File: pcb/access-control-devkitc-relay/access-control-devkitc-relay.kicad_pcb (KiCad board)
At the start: 2 copper layers, 21.2 x 56 mm, 12 parts, among them K1 G5LE-1

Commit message: Update with values
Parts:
- added D3: D_Zener, Diode_THT:D_DO-41_SOD81_P10.16mm_Horizontal, F.Cu at (19.0, 27.4)
- moved J_COIL_LOW1 15.7 mm to (18.9, 34.2)
- renumbered J_COIL_LOW1 to J_COIL_HIGH1, J_COIL_LOW2 to J_COIL_LOW1
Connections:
- J_COIL_LOW1 pad 1: Net-(D1-A) -> Net-(D3-K)
- K1 pad 2: Net-(D1-A) -> Net-(D3-K)
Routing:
- net Net-(D3-K): track 0.00 -> 36.2 mm
- net Net-(D1-A): track 24.7 -> 2.61 mm

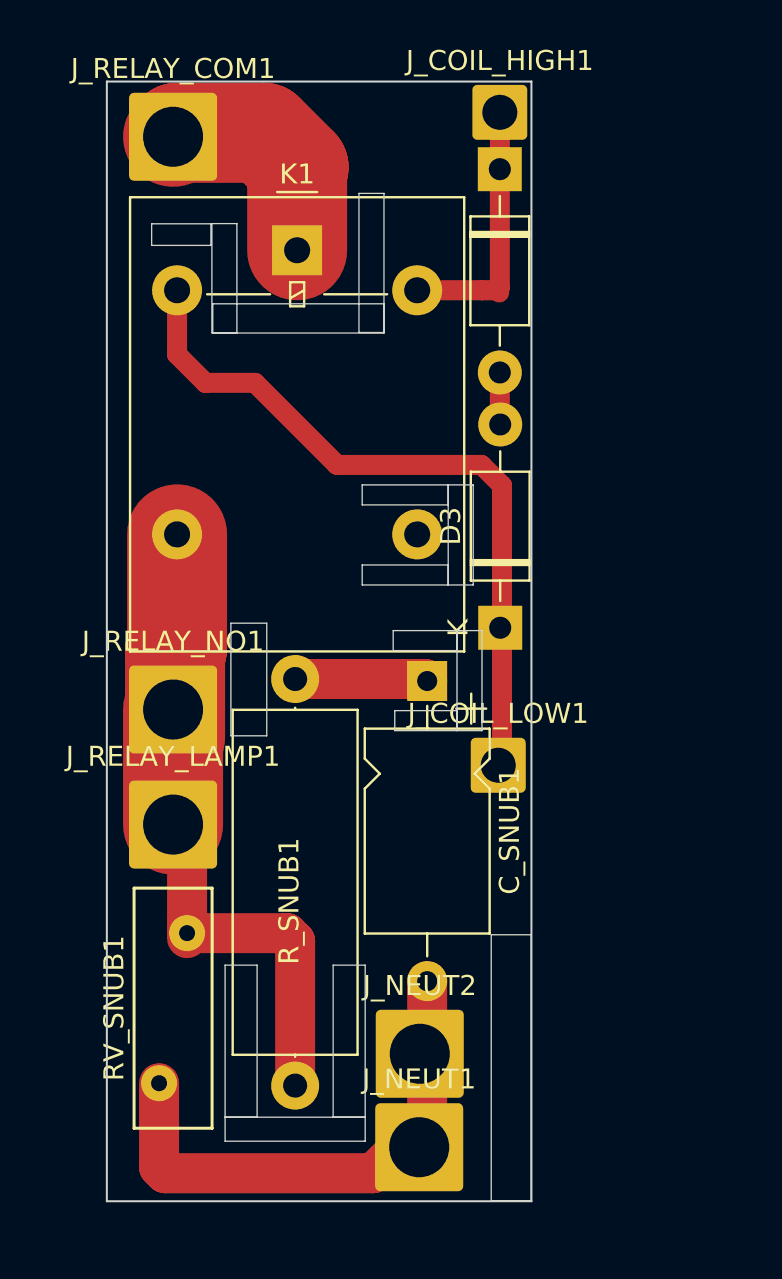
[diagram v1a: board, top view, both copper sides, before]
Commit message: Contactor interface and current sensor (part only)
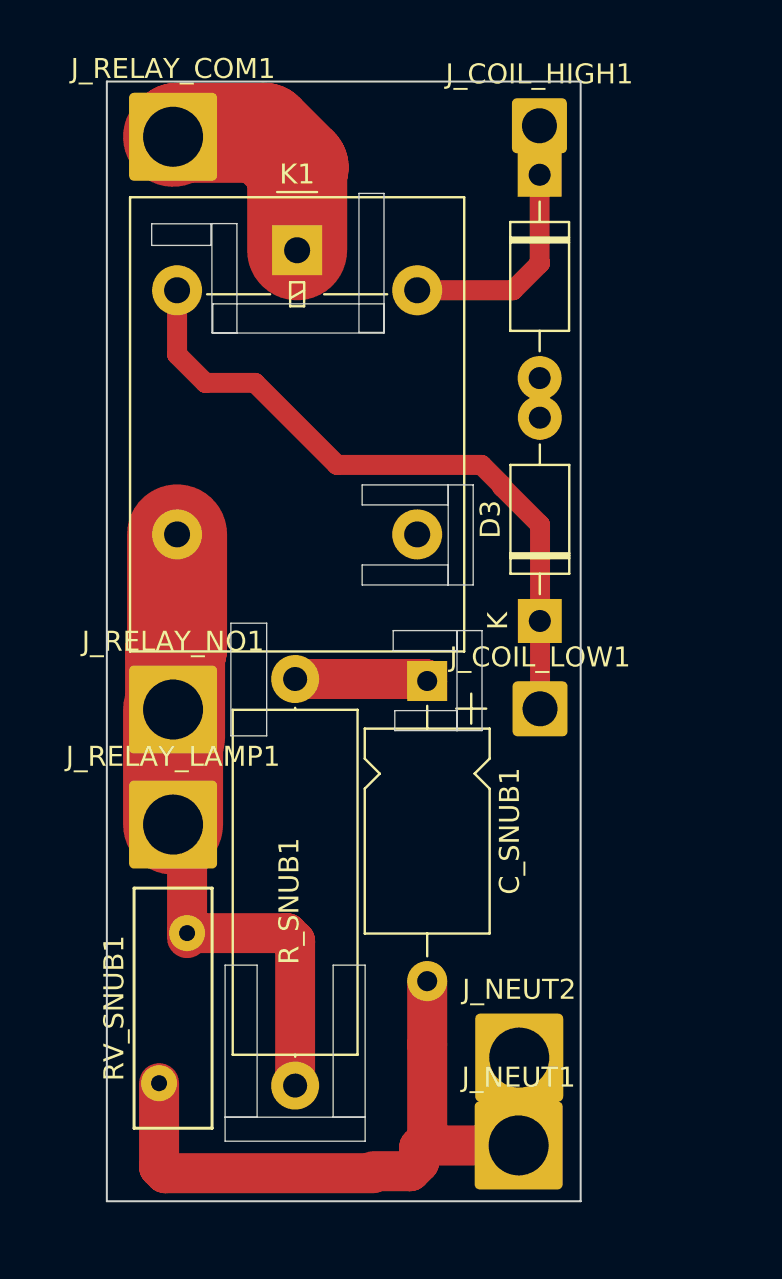
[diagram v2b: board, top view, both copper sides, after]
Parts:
- moved J_NEUT2 4.97 mm to (19.9, 48.8)
- moved J_NEUT1 4.97 mm to (19.9, 53.2)
- moved J_COIL_LOW1 3.51 mm to (21.0, 31.4)
- moved J_COIL_HIGH1 2.09 mm to (21.0, 2.27)
- moved D1 2.01 mm to (21.0, 4.72)
- moved D3 2.01 mm to (21.0, 27.0)
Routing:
- net NEUT: track 25.0 -> 36.1 mm
- net Net-(D3-K): track 36.2 -> 34.1 mm
- net +5V: track 12.8 -> 14.0 mm
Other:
- board size 21.2 x 56 mm -> 23.7 x 56 mm

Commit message: Fixes to relief, JST connectors for SMT board
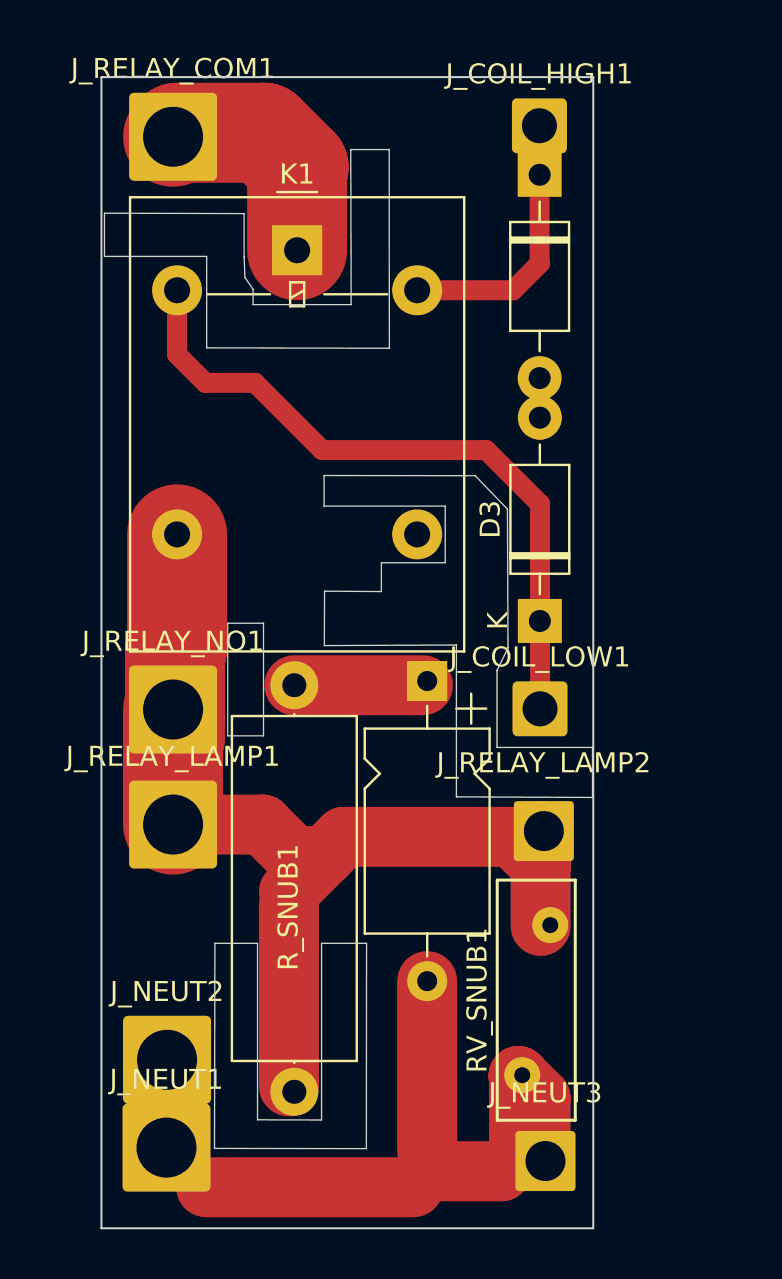
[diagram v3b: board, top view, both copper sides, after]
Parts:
- added J_NEUT3: Conn_01x01_Socket, Connector_Wire:SolderWire-2.5sqmm_1x01_D2.4mm_OD4.4mm, F.Cu at (21.3, 54.0)
- added J_RELAY_LAMP2: Conn_01x01_Socket, Connector_Wire:SolderWire-2.5sqmm_1x01_D2.4mm_OD4.4mm, F.Cu at (21.2, 37.5)
- moved RV_SNUB1 18.2 mm to (21.5, 42.2)
- moved J_NEUT1 17.6 mm to (2.32, 53.3)
- moved J_NEUT2 17.6 mm to (2.35, 49.0)
- moved R_SNUB1 0.31 mm to (8.71, 50.5)
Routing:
- net Net-(J_RELAY_LAMP1-Pin_1): track 36.5 -> 55.0 mm
- net Net-(D1-A): track 2.61 -> 4.59 mm
- net NEUT: track 36.1 -> 38.0 mm
- net Net-(D3-K): track 34.1 -> 34.7 mm
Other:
- board size 23.7 x 56 mm -> 24.6 x 57.5 mm

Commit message: Final changes pre manufacture
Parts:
- added CON_DAISY1: Conn_01x04_Socket, Connector_JST:JST_XA_B04B-XASK-1_1x04_P2.50mm_Vertical, F.Cu at (27.0, 22.7)
- added CON_MCU1: Conn_01x04_Socket, Connector_PinHeader_2.54mm:PinHeader_1x04_P2.54mm_Vertical, F.Cu at (26.3, 10.2)
- added CON_PWR1: Conn_01x02_Socket, Connector_JST:JST_XH_B2B-XH-A_1x02_P2.50mm_Vertical, F.Cu at (27.0, 2.80)
- added C_5V_Large1: 1000uf, Capacitor_THT:CP_Radial_D8.0mm_P5.00mm, F.Cu at (23.7, 15.0)
- added JP1: SolderJumper_2_Open, Jumper:SolderJumper-2_P1.3mm_Open_TrianglePad1.0x1.5mm, F.Cu at (23.5, 19.1)
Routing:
- net +5V: track 14.0 -> 51.3 mm
- net GND: track 0.00 -> 29.1 mm
- net Net-(CON_DAISY1-Pin_4): track 0.00 -> 16.2 mm
- net Net-(CON_DAISY1-Pin_3): track 34.7 -> 43.9 mm
- net Net-(CON_MCU1-Pin_3): track 0.00 -> 4.37 mm
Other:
- board size 24.6 x 57.5 mm -> 31.9 x 57.5 mm
- board text added: "devkitc-relay V1 2025-05-20"

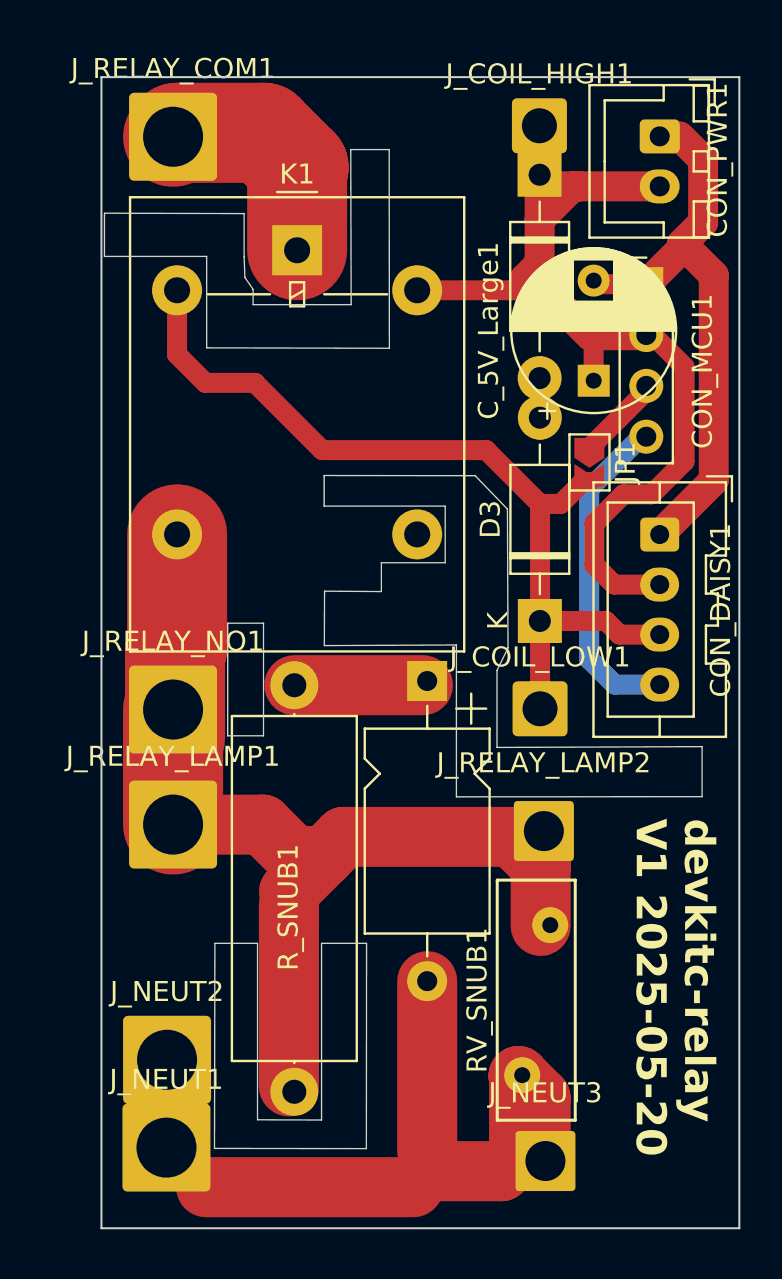
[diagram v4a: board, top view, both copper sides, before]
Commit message: Pads for TWI, space for 5v signal option
Copper on the back of relay
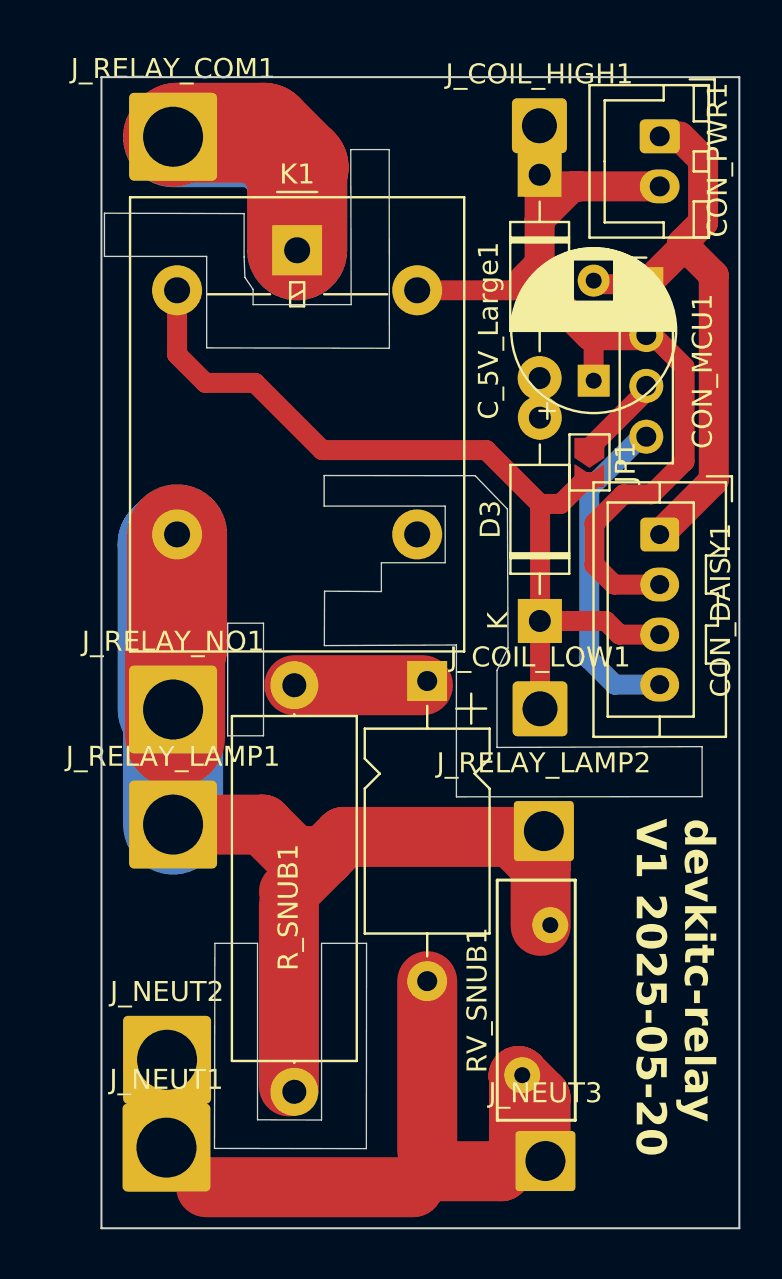
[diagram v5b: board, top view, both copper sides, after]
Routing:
- net Net-(J_RELAY_COM1-Pin_1): track 11.2 -> 22.2 mm
- net Net-(J_RELAY_LAMP1-Pin_1): track 55.0 -> 63.9 mm
